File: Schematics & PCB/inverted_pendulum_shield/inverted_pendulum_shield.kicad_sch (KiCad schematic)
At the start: 48 parts, among them J1 Screw_Terminal_01x02, J2 Screw_Terminal_01x04, J3 Screw_Terminal_01x02, J4 FCR7350R, J5 FCR7350B, Q1 DMP3056L-7, Q2 NX138BKR, Q3 FQD8P10TM, Q4 SLMT320V3CN, Q5 SLMT320V3CN, SW1 1825027, U1 DRV8231DDAR, U2 AP63301WU-7

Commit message: finished revision 2 of pcb and schematics
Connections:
- net Controls Start: now also A1.14 (GPIO10); no longer A1.21 (GPIO16)
- net LED_indicate: now also A1.15 (GPIO11); no longer A1.24 (GPIO18)
- net Motor Control 1: now also A1.26 (GPIO20); no longer A1.11 (GPIO8)
- net Motor Control 2: now also A1.27 (GPIO21); no longer A1.12 (GPIO9)
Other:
- note removed: "need to get footprint for pot"
- company: (none) -> Group 22
- title: Reaction-Wheel-Inverted-Pendulum Shield  -> Reaction Wheel Inverted Pendulum Shield
- moved on the sheet: D1, R7

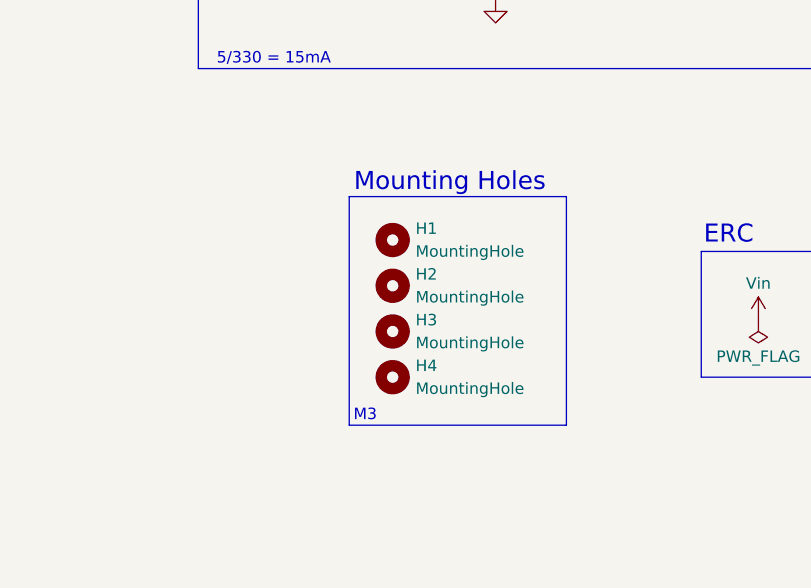
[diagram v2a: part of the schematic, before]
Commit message: Finished BOM and finalised PCB layout
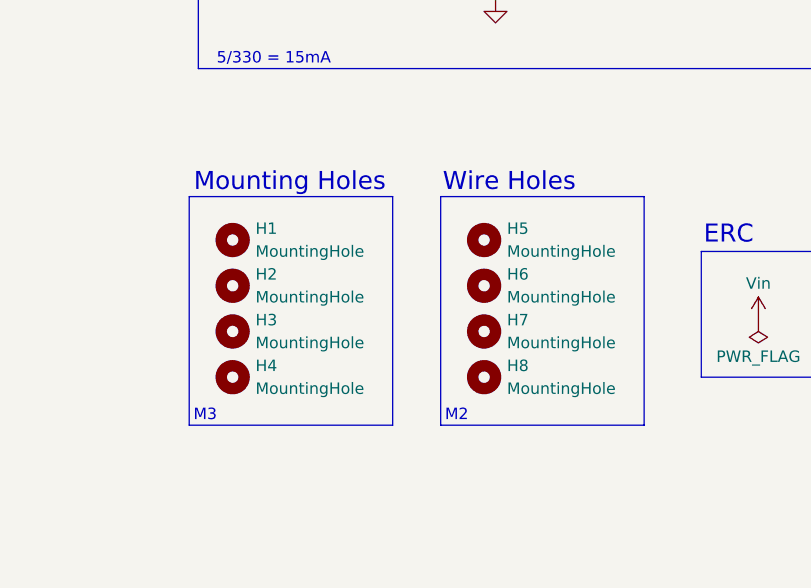
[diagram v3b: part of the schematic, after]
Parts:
- added H5, H6, H7, H8: MountingHole, MountingHole:MountingHole_3.2mm_M3, symbol Mechanical:MountingHole
- D1: footprint Resistor_SMD:R_0603_1608Metric -> LED_SMD:LED_0603_1608Metric
- D5: footprint Resistor_SMD:R_0805_2012Metric -> LED_SMD:LED_0805_2012Metric
- J4: footprint Connector:Banana_Cliff_FCR7350R_S16N-PC_Horizontal -> Connector_Wire:SolderWirePad_1x01_SMD_4x8mm
- J5: footprint Connector:Banana_Cliff_FCR7350B_S16N-PC_Horizontal -> Connector_Wire:SolderWirePad_1x01_SMD_4x8mm
- Q3: footprint Package_TO_SOT_SMD:TO-252-2_TabPin1 -> Package_TO_SOT_SMD:TO-252-2
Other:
- note added: "M2"
- note added: "Wire Holes"
- moved on the sheet: H1, H2, H3, H4

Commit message: Finished final schematic and PCB revisions
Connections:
- net VM: now reaches C1.1, C2.1, Q1.1 (D), U1.5 (VM)
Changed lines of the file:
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@@
+		)
+	)
+	(label "VM"
+		(at 73.66 58.42 270)
+		(effects
+			(font
+				(size 0.635 0.635)
+			)
+			(justify right bottom)
 		)
 	)
